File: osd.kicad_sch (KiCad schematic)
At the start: 9 parts

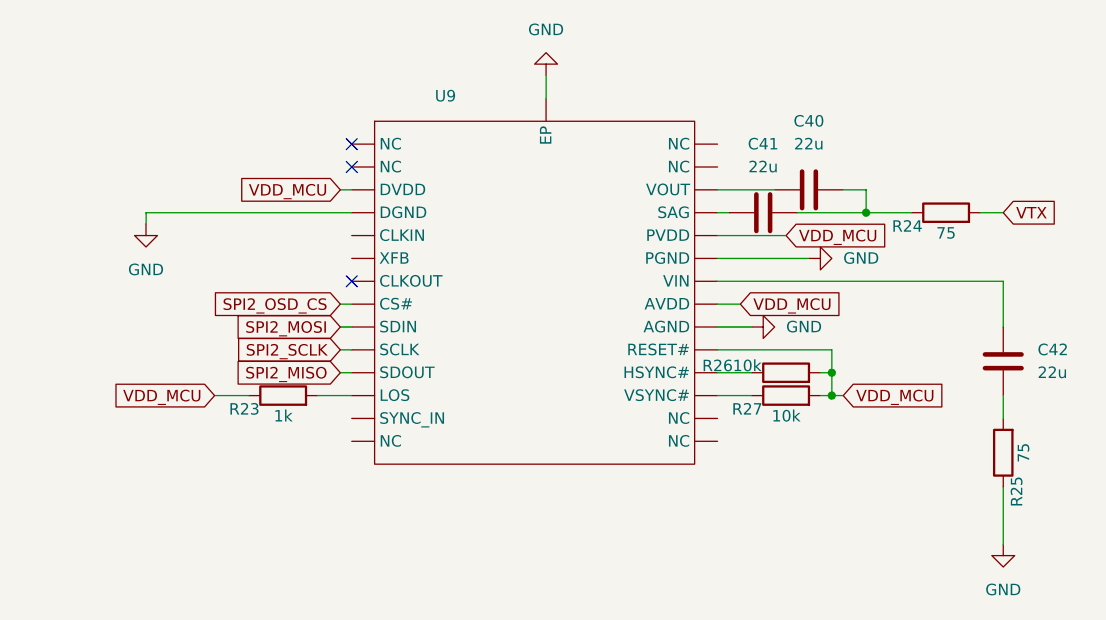
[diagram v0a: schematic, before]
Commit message: finished blackbox led and osd, then started rx
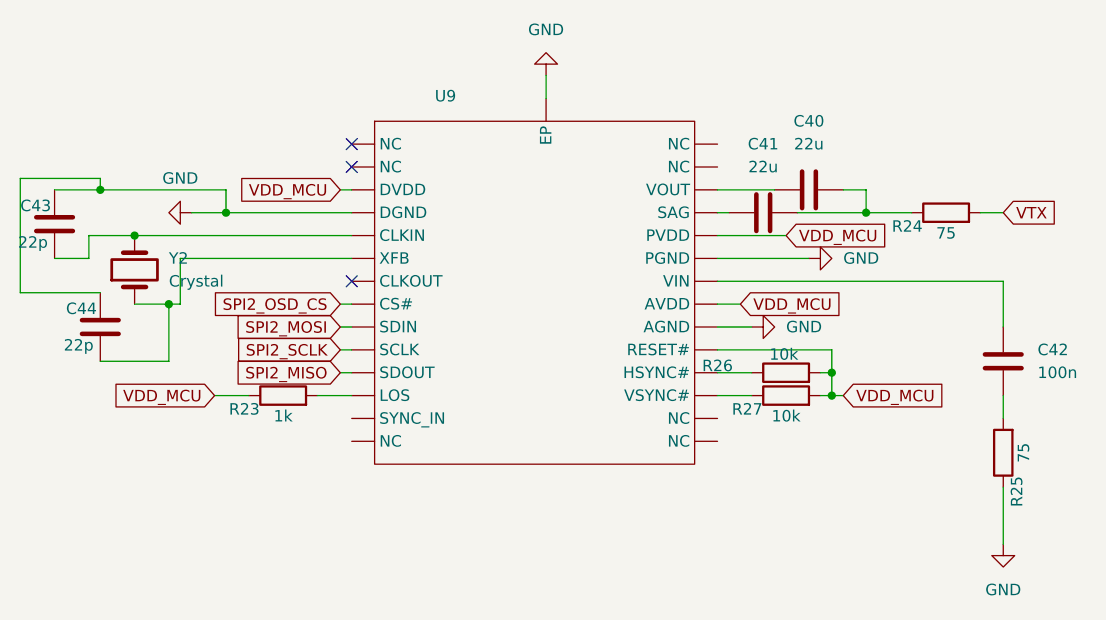
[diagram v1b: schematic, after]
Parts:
- added C43, C44: 22p, symbol Device:C
- added Y2: Crystal, symbol Device:Crystal
- C42: value 22u -> 100n
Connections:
- net GND: now also C43.2, C44.2
- new net: C43.1, U9. (NC), Y2.2
- new net: C44.1, U9. (NC), Y2.1

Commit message: refactor labels U and assigned resistance footprint
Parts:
- R23, R24, R25, R26, R27: footprint (none) -> Resistor_SMD:R_0603_1608Metric
- U8: renamed from U9; value ~ -> AT7456E
- Y2: Fréquence (none) -> 27M
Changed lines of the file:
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@@
 			)
 		)
-		(property "Footprint" ""
+		(property "Footprint" "Resistor_SMD:R_0603_1608Metric"
 			(at 71.12 80.518 90)
 			(effects
@@
 			)
 		)
-		(property "Footprint" ""
+		(property "Footprint" "Resistor_SMD:R_0603_1608Metric"
 			(at 127 80.518 90)
 			(effects
@@
 			)
 		)
-		(property "Footprint" ""
+		(property "Footprint" "Resistor_SMD:R_0603_1608Metric"
 			(at 144.78 60.198 90)
 			(effects
@@
 		(on_board yes)
 		(dnp no)
-		(property "Reference" "U9"
-			(at 89.154 45.466 0)
-			(effects
-				(font
-					(size 1.27 1.27)
-				)
-			)
-		)
-		(property "Value" "~"
-			(at 83.82 47.244 0)
+		(property "Reference" "U8"
+			(at 88.9 44.704 0)
+			(effects
+				(font
+					(size 1.27 1.27)
+				)
+			)
+		)
+		(property "Value" "AT7456E"
+			(at 89.154 47.244 0)
 			(effects
 				(font
@@
 			)
 		)
-		(property "Description" ""
-			(at 80.01 46.99 0)
-			(effects
-				(font
-					(size 1.27 1.27)
-				)
-				(hide yes)
+		(property "Description" "OSD"
+			(at 105.918 46.736 0)
+			(effects
+				(font
+					(size 1.27 1.27)
+				)
 			)
 		)
@@
 			(project ""
 				(path "/11716af6-0e6e-444b-b738-3f12da23c1a2/636c513f-d8b7-45ca-ba45-01de0ad6adcc"
-					(reference "U9")
+					(reference "U8")
 					(unit 1)
 				)
@@
 			)
 		)
-		(property "Footprint" ""
+		(property "Footprint" "Resistor_SMD:R_0603_1608Metric"
 			(at 152.908 85.09 90)
 			(effects
@@
 			)
 		)
-		(property "Footprint" ""
+		(property "Footprint" "Resistor_SMD:R_0603_1608Metric"
 			(at 127 77.978 90)
 			(effects
@@
 		(on_board yes)
 		(dnp no)
-		(fields_autoplaced yes)
 		(property "Reference" "Y2"
 			(at 58.42 63.4999 90)
@@
 			)
 		)
+		(property "Fréquence" "27M"
+			(at 49.53 65.278 90)
+			(effects
+				(font
+					(size 1.27 1.27)
+				)
+			)
+		)

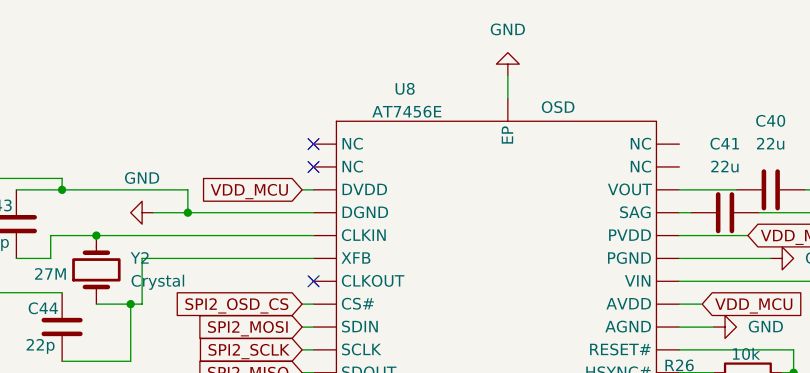
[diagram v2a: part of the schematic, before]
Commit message: refactor and update references, added some footprints
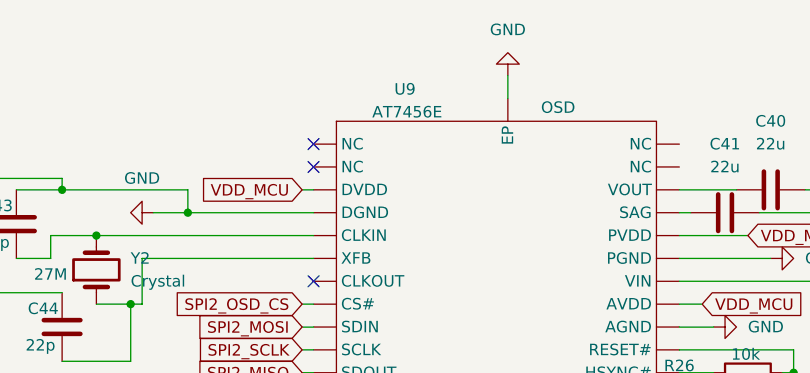
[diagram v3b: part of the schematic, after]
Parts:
- C40, C41: footprint (none) -> Capacitor_SMD:C_1210_3225Metric
- C42, C43, C44: footprint (none) -> Capacitor_SMD:C_0603_1608Metric
- Y2: footprint (none) -> Crystal:Crystal_SMD_3225-4Pin_3.2x2.5mm
- renumbered U8 to U9
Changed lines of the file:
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@@
 			)
 		)
-		(property "Footprint" ""
+		(property "Footprint" "Capacitor_SMD:C_1210_3225Metric"
 			(at 133.35 54.9148 0)
 			(effects
@@
 		(on_board yes)
 		(dnp no)
-		(property "Reference" "U8"
+		(property "Reference" "U9"
 			(at 88.9 44.704 0)
 			(effects
@@
 			(project ""
 				(path "/11716af6-0e6e-444b-b738-3f12da23c1a2/636c513f-d8b7-45ca-ba45-01de0ad6adcc"
-					(reference "U8")
+					(reference "U9")
 					(unit 1)
 				)
@@
 			)
 		)
-		(property "Footprint" ""
+		(property "Footprint" "Capacitor_SMD:C_0603_1608Metric"
 			(at 150.1648 71.12 0)
 			(effects
@@
 			)
 		)
-		(property "Footprint" ""
+		(property "Footprint" "Capacitor_SMD:C_0603_1608Metric"
 			(at 44.7548 55.88 0)
 			(effects
@@
 			)
 		)
-		(property "Footprint" ""
+		(property "Footprint" "Capacitor_SMD:C_1210_3225Metric"
 			(at 128.27 57.4548 0)
 			(effects
@@
 			)
 		)
-		(property "Footprint" ""
+		(property "Footprint" "Crystal:Crystal_SMD_3225-4Pin_3.2x2.5mm"
 			(at 54.61 64.77 0)
 			(effects
@@
 			)
 		)
-		(property "Footprint" ""
+		(property "Footprint" "Capacitor_SMD:C_0603_1608Metric"
 			(at 49.8348 67.31 0)
 			(effects
